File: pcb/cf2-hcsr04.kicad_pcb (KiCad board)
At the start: 2 copper layers, 25.2 x 27.3 mm, 9 parts, among them P1 CF_EXP_LEFT, P2 CF_EXP_RIGHT, U1 DS28E05, U2 REG71050, U3 HC-SR04

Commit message: First pcb draft
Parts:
- P1: footprint connectors:BF090-10-X-B2 -> connectors:BF090-10-X-B2-LEFT-NOPADS
- P2: footprint connectors:BF090-10-X-B2 -> connectors:BF090-10-X-B2-RIGHT-NOPADS
- moved U1 20.3 mm to (128.5, 103.9), turned to 90 degrees
- moved C2 9.99 mm to (140.5, 103.1), turned to 0 degrees
- moved U3 9.92 mm to (146.6, 97.0), turned to 270 degrees
- moved C1 2.29 mm to (141.7, 97.8)
- moved C3 0.37 mm to (135.9, 96.5)
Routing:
- net GND: track 22.8 -> 71.7 mm, vias 2 -> 0
- net /IO_4: track 49.7 -> 10.5 mm
- net /IO_1: track 5.67 -> 20.9 mm
- net /IO_2: track 5.37 -> 20.2 mm
- net /OW: track 18.8 -> 11.1 mm
- net /VCOM: track 13.8 -> 20.9 mm
- net N-0000021: track 9.82 -> 3.64 mm, vias 2 -> 0
- net N-0000022: track 24.3 -> 29.7 mm, vias 0 -> 4
- removed copper zone on B.Cu, net GND
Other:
- net class Default: clearance 0.1524 -> 0.0254; trace_width 0.2032 -> 0.508
- rule trace_clearance: 0.1524 -> 0.0254
- rule trace_min: 0.1524 -> 0.254

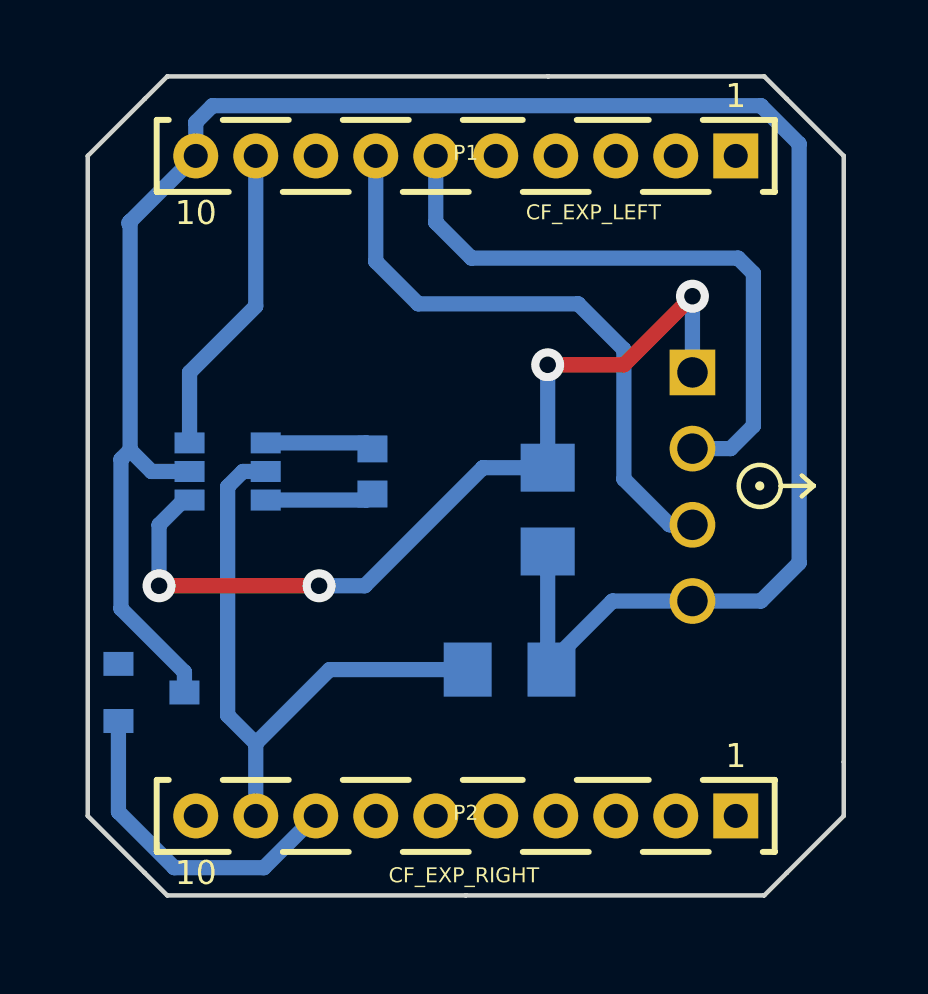
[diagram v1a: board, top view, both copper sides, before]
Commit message: Improved thickness of vias and other connections
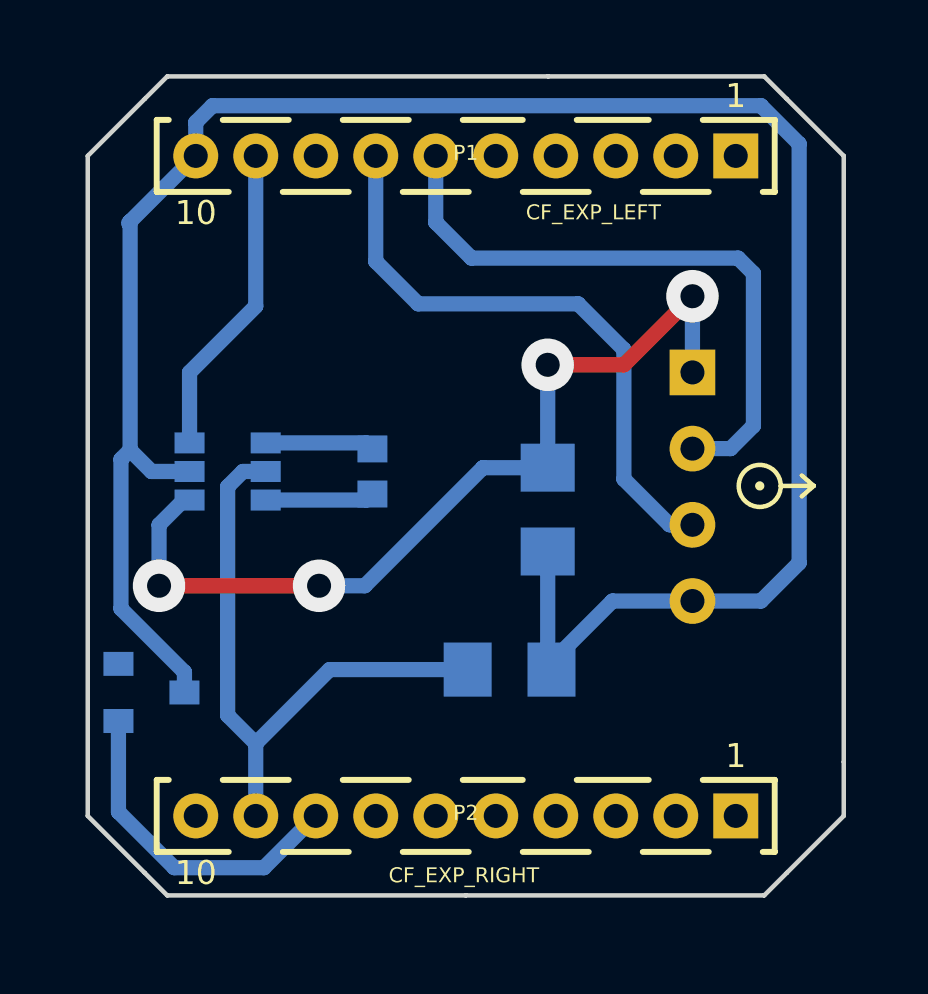
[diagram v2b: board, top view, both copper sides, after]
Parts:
- U3: footprint PIN_ARRAY_4x1 -> HC-SR04
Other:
- net class Default: via_dia 1.1 -> 1.75; via_drill 1 -> 0.8
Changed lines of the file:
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@@
     (segment_width 0.2)
     (edge_width 0.15)
-    (via_size 1.1)
-    (via_drill 1)
+    (via_size 1.75)
+    (via_drill 0.8)
     (via_min_size 0.635)
     (via_min_drill 0.381)
@@
     (mod_text_size 1 1)
     (mod_text_width 0.15)
-    (pad_size 1.5 1.5)
+    (pad_size 1.524 1.524)
     (pad_drill 0.8)
     (pad_to_mask_clearance 0)
@@
     (clearance 0.0254)
     (trace_width 0.508)
-    (via_dia 1.1)
-    (via_drill 1)
+    (via_dia 1.75)
+    (via_drill 0.8)
     (uvia_dia 0.6)
     (uvia_drill 0.5)
@@
       (scale (xyz 0.4 0.4 0.4))
       (rotate (xyz 0 0 180))
-    )
-  )
-  (module PIN_ARRAY_4x1 (layer B.Cu)
-    (at 146.558 97.028 270)
-    (descr "Double rangee de contacts 2 x 5 pins")
-    (tags CONN)
-    (fp_text reference U3 (at 0 2.54 270) (layer B.SilkS)
-      (effects (font (size 1.016 1.016) (thickness 0.2032)) (justify mirror))
-    )
-    (fp_text value HC-SR04 (at -0.254 2.54 270) (layer B.SilkS) hide
-      (effects (font (size 0.7 0.7) (thickness 0.15)) (justify mirror))
-    )
-    (fp_line (start 5.08 -1.27) (end -5.08 -1.27) (layer B.SilkS) (width 0.254))
-    (fp_line (start 5.08 1.27) (end -5.08 1.27) (layer B.SilkS) (width 0.254))
-    (fp_line (start -5.08 1.27) (end -5.08 -1.27) (layer B.SilkS) (width 0.254))
-    (fp_line (start 5.08 -1.27) (end 5.08 1.27) (layer B.SilkS) (width 0.254))
-    (pad 1 thru_hole rect (at -3.81 0 270) (size 1.524 1.524) (drill 1.016)
-      (layers *.Cu *.Mask B.SilkS)
-      (net 8 N-0000022)
-    )
-    (pad 2 thru_hole circle (at -1.27 0 270) (size 1.524 1.524) (drill 1.016)
-      (layers *.Cu *.Mask B.SilkS)
-      (net 1 /IO_1)
-    )
-    (pad 3 thru_hole circle (at 1.27 0 270) (size 1.524 1.524) (drill 1.016)
-      (layers *.Cu *.Mask B.SilkS)
-      (net 2 /IO_2)
-    )
-    (pad 4 thru_hole circle (at 3.81 0 270) (size 1.524 1.524) (drill 1.016)
-      (layers *.Cu *.Mask B.SilkS)
-      (net 6 GND)
-    )
-    (model pin_array\pins_array_4x1.wrl
-      (at (xyz 0 0 0))
-      (scale (xyz 1 1 1))
-      (rotate (xyz 0 0 0))
     )
   )
@@
     (pad 5 thru_hole circle (at -1 0 180) (size 1.5 1.5) (drill 0.8)
       (layers *.Cu *.Mask F.SilkS)
+    )
+  )
+  (module HC-SR04 (layer B.Cu)
+    (at 146.558 97.028 270)
+    (descr "Double rangee de contacts 2 x 5 pins")
+    (tags CONN)
+    (fp_text reference U3 (at 0 2.54 270) (layer B.SilkS)
+      (effects (font (size 1.016 1.016) (thickness 0.2032)) (justify mirror))
+    )
+    (fp_text value HC-SR04 (at 0 -2.54 270) (layer B.SilkS) hide
+      (effects (font (size 1.016 1.016) (thickness 0.2032)) (justify mirror))
+    )
+    (fp_line (start 5.08 -1.27) (end -5.08 -1.27) (layer B.SilkS) (width 0.254))
+    (fp_line (start 5.08 1.27) (end -5.08 1.27) (layer B.SilkS) (width 0.254))
+    (fp_line (start -5.08 1.27) (end -5.08 -1.27) (layer B.SilkS) (width 0.254))
+    (fp_line (start 5.08 -1.27) (end 5.08 1.27) (layer B.SilkS) (width 0.254))
+    (pad 1 thru_hole rect (at -3.81 0 270) (size 1.524 1.524) (drill 0.8)
+      (layers *.Cu *.Mask B.SilkS)
+      (net 8 N-0000022)
+    )
+    (pad 2 thru_hole circle (at -1.27 0 270) (size 1.524 1.524) (drill 0.8)
+      (layers *.Cu *.Mask B.SilkS)
+      (net 1 /IO_1)
+    )
+    (pad 3 thru_hole circle (at 1.27 0 270) (size 1.524 1.524) (drill 0.8)
+      (layers *.Cu *.Mask B.SilkS)
+      (net 2 /IO_2)
+    )
+    (pad 4 thru_hole circle (at 3.81 0 270) (size 1.524 1.524) (drill 0.8)
+      (layers *.Cu *.Mask B.SilkS)
+      (net 6 GND)
+    )
+    (model pin_array\pins_array_4x1.wrl
+      (at (xyz 0 0 0))
+      (scale (xyz 1 1 1))
+      (rotate (xyz 0 0 0))
     )
   )
@@
   (segment (start 146.558 93.218) (end 146.558 90.678) (width 0.508) (layer B.Cu) (net 8))
   (segment (start 141.732 92.964) (end 141.732 96.393) (width 0.508) (layer B.Cu) (net 8))
-  (via (at 141.732 92.964) (size 1.1) (layers F.Cu B.Cu) (net 8))
+  (via (at 141.732 92.964) (size 1.75) (layers F.Cu B.Cu) (net 8))
   (segment (start 144.272 92.964) (end 141.732 92.964) (width 0.508) (layer F.Cu) (net 8))
   (segment (start 146.558 90.678) (end 144.272 92.964) (width 0.508) (layer F.Cu) (net 8))
-  (via (at 146.558 90.678) (size 1.1) (layers F.Cu B.Cu) (net 8))
+  (via (at 146.558 90.678) (size 1.75) (layers F.Cu B.Cu) (net 8))
   (segment (start 134.112 100.33) (end 135.636 100.33) (width 0.508) (layer B.Cu) (net 8))
-  (via (at 128.778 100.33) (size 1.1) (layers F.Cu B.Cu) (net 8))
+  (via (at 128.778 100.33) (size 1.75) (layers F.Cu B.Cu) (net 8))
   (segment (start 128.778 100.33) (end 134.112 100.33) (width 0.508) (layer F.Cu) (net 8))
-  (via (at 134.112 100.33) (size 1.1) (layers F.Cu B.Cu) (net 8))
+  (via (at 134.112 100.33) (size 1.75) (layers F.Cu B.Cu) (net 8))
   (segment (start 128.778 98.298) (end 128.778 100.33) (width 0.508) (layer B.Cu) (net 8))
   (segment (start 129.6035 97.4725) (end 128.778 98.298) (width 0.508) (layer B.Cu) (net 8))

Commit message: Added side information and text to footprint (fixes #1)
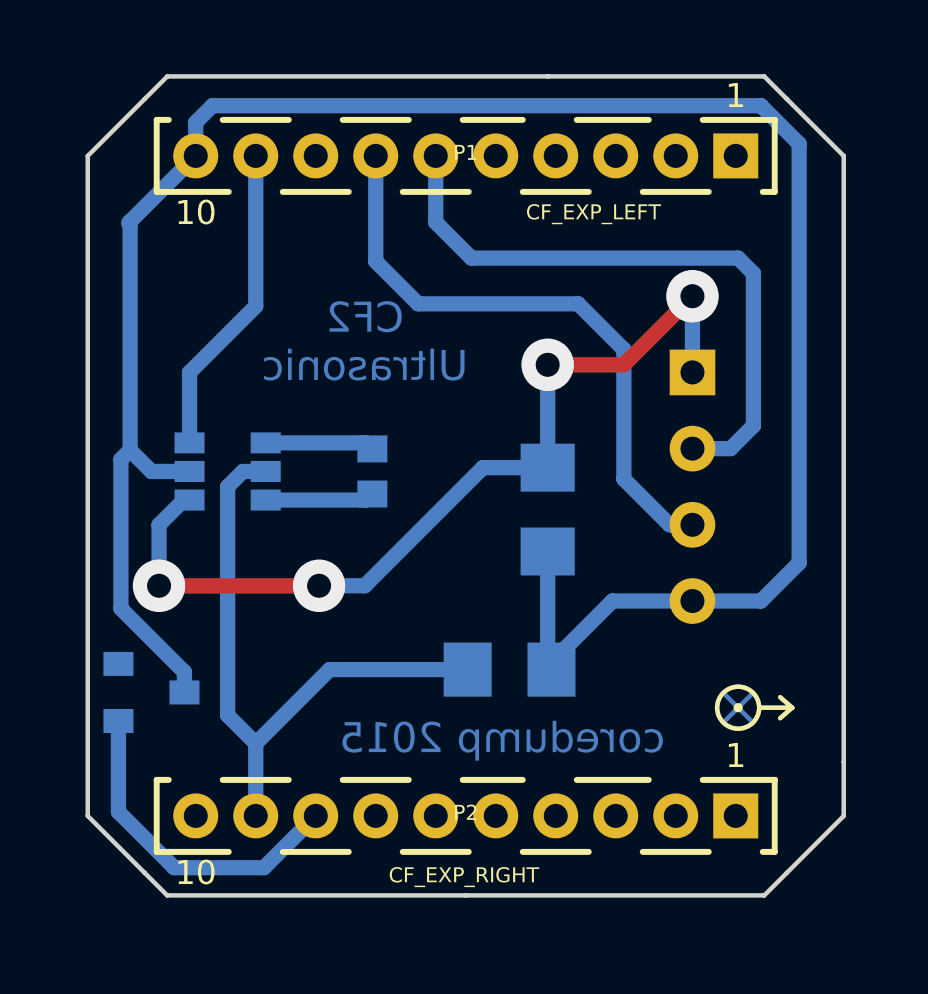
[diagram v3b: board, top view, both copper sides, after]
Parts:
- moved EXP_ORIENTATION 7.43 mm to (148.1, 104.4)
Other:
- board text added: "CF2 Ultrasonic"
- board text added: "coredump 2015"
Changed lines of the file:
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@@
     (area 82.650999 40.650919 195.351001 153.350921)
     (thickness 1.6)
-    (drawings 1896)
+    (drawings 1898)
     (tracks 66)
     (zones 0)
@@
   )
   (setup
-    (last_trace_width 0.508)
+    (last_trace_width 1)
     (user_trace_width 0.254)
     (user_trace_width 0.508)
@@
     )
   )
-  (module bitcraze:EXP_ORIENTATION_B_MASK (layer F.Cu)
-    (at 148.801 97.00092)
-    (fp_text reference EXP_ORIENTATION (at 0 1.925) (layer F.SilkS) hide
-      (effects (font (size 1 1) (thickness 0.15)))
-    )
-    (fp_text value VAL** (at 0.043 1.80508) (layer F.SilkS) hide
-      (effects (font (size 1 1) (thickness 0.15)))
-    )
-    (fp_line (start 0 0) (end -0.475 0.475) (layer B.Mask) (width 0.15))
-    (fp_line (start 0 0) (end 0.475 0.475) (layer B.Mask) (width 0.15))
-    (fp_line (start 0 0) (end 0.475 -0.475) (layer B.Mask) (width 0.15))
-    (fp_line (start 0 0) (end -0.475 -0.475) (layer B.Mask) (width 0.15))
-    (fp_circle (center 0 0) (end 0.7 0.025) (layer B.Mask) (width 0.15))
-    (fp_line (start 0.7 0) (end 1.8 0) (layer B.Mask) (width 0.15))
-    (fp_line (start 1.8 0) (end 1.4 -0.35) (layer B.Mask) (width 0.15))
-    (fp_line (start 1.8 0) (end 1.4 0.35) (layer B.Mask) (width 0.15))
-    (fp_line (start 1.8 0) (end 1.4 0.35) (layer F.SilkS) (width 0.15))
-    (fp_line (start 1.8 0) (end 1.4 -0.35) (layer F.SilkS) (width 0.15))
-    (fp_line (start 0.7 0) (end 1.8 0) (layer F.SilkS) (width 0.15))
-    (fp_circle (center 0 0) (end 0.7 0.025) (layer F.SilkS) (width 0.15))
-    (fp_circle (center 0 0) (end 0.075 0.025) (layer F.SilkS) (width 0.15))
-  )
   (module connectors:BF090-10-X-B2-LEFT-NOPADS (layer F.Cu)
     (at 139.001 86.00092 180)
@@
     )
   )
+  (module bitcraze:EXP_ORIENTATION_B_MASK (layer F.Cu)
+    (at 148.082 104.394)
+    (fp_text reference EXP_ORIENTATION (at 0 1.925) (layer F.SilkS) hide
+      (effects (font (size 1 1) (thickness 0.15)))
+    )
+    (fp_text value VAL** (at -1.27 -1.27) (layer F.SilkS) hide
+      (effects (font (size 1 1) (thickness 0.15)))
+    )
+    (fp_line (start 0 0) (end -0.475 0.475) (layer B.Cu) (width 0.15))
+    (fp_line (start 0 0) (end 0.475 0.475) (layer B.Cu) (width 0.15))
+    (fp_line (start 0 0) (end 0.475 -0.475) (layer B.Cu) (width 0.15))
+    (fp_line (start 0 0) (end -0.475 -0.475) (layer B.Cu) (width 0.15))
+    (fp_circle (center 0 0) (end 0.7 0.025) (layer B.Cu) (width 0.15))
+    (fp_line (start 0.7 0) (end 1.8 0) (layer B.Cu) (width 0.15))
+    (fp_line (start 1.8 0) (end 1.4 -0.35) (layer B.Cu) (width 0.15))
+    (fp_line (start 1.8 0) (end 1.4 0.35) (layer B.Cu) (width 0.15))
+    (fp_line (start 1.8 0) (end 1.4 0.35) (layer F.SilkS) (width 0.15))
+    (fp_line (start 1.8 0) (end 1.4 -0.35) (layer F.SilkS) (width 0.15))
+    (fp_line (start 0.7 0) (end 1.8 0) (layer F.SilkS) (width 0.15))
+    (fp_circle (center 0 0) (end 0.7 0.025) (layer F.SilkS) (width 0.15))
+    (fp_circle (center 0 0) (end 0.075 0.025) (layer F.SilkS) (width 0.15))
+  )
+  (gr_text "coredump 2015" (at 140.208 105.41) (layer B.Cu)
+    (effects (font (size 1 1) (thickness 0.25)) (justify mirror))
+  )
+  (gr_text "CF2\nUltrasonic" (at 135.636 92.202) (layer B.Cu)
+    (effects (font (size 1 1) (thickness 0.25)) (justify mirror))
+  )
   (gr_circle (center 171.751 129.75092) (end 148.251 129.75092) (layer Eco1.User) (width 0.2))

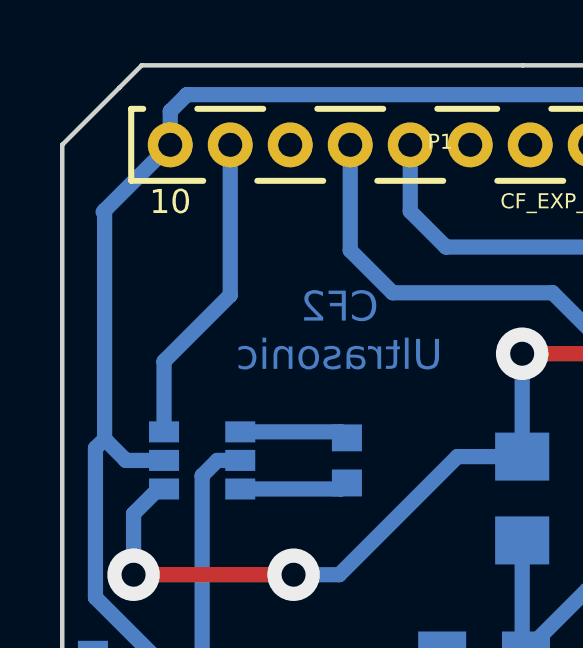
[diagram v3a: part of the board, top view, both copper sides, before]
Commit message: Removed acute angle
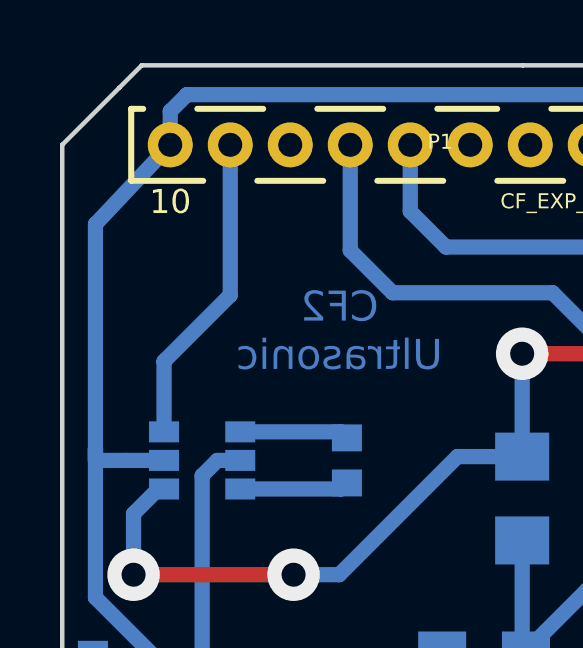
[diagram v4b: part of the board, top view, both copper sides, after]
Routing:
- net GND: track 71.7 -> 72.4 mm
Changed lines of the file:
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@@
     (thickness 1.6)
     (drawings 1898)
-    (tracks 66)
+    (tracks 65)
     (zones 0)
     (modules 9)
@@
   )
   (setup
-    (last_trace_width 1)
+    (last_trace_width 0.508)
     (user_trace_width 0.254)
     (user_trace_width 0.508)
@@
   (segment (start 131.572 96.52) (end 131.064 97.028) (width 0.508) (layer B.Cu) (net 5))
   (segment (start 129.62382 103.886) (end 129.62382 103.20782) (width 0.508) (layer B.Cu) (net 6))
-  (segment (start 127.508 96.11392) (end 127.81296 95.80896) (width 0.508) (layer B.Cu) (net 6))
+  (segment (start 127.508 96.11392) (end 127.508 96.52) (width 0.508) (layer B.Cu) (net 6))
   (segment (start 127.508 101.092) (end 127.508 96.11392) (width 0.508) (layer B.Cu) (net 6))
   (segment (start 129.62382 103.20782) (end 127.508 101.092) (width 0.508) (layer B.Cu) (net 6))
@@
   (segment (start 130.556 84.328) (end 148.844 84.328) (width 0.508) (layer B.Cu) (net 6))
   (segment (start 130.001 84.883) (end 130.556 84.328) (width 0.508) (layer B.Cu) (net 6))
-  (segment (start 127.81296 88.18896) (end 127.81296 95.80896) (width 0.508) (layer B.Cu) (net 6))
+  (segment (start 127.508 88.646) (end 127.508 96.52) (width 0.508) (layer B.Cu) (net 6))
   (segment (start 128.524 96.52) (end 129.794 96.52) (width 0.508) (layer B.Cu) (net 6))
-  (segment (start 127.81296 95.80896) (end 128.524 96.52) (width 0.508) (layer B.Cu) (net 6))
+  (segment (start 127.508 96.52) (end 128.524 96.52) (width 0.508) (layer B.Cu) (net 6))
   (segment (start 141.732 99.187) (end 141.732 102.997) (width 0.508) (layer B.Cu) (net 6) (status 10))
   (segment (start 141.732 102.997) (end 143.891 100.838) (width 0.508) (layer B.Cu) (net 6))
   (segment (start 143.891 100.838) (end 146.558 100.838) (width 0.508) (layer B.Cu) (net 6))
-  (segment (start 127.762 88.23992) (end 127.81296 88.18896) (width 0.508) (layer B.Cu) (net 6))
-  (segment (start 127.81296 88.18896) (end 130.001 86.00092) (width 0.508) (layer B.Cu) (net 6))
+  (segment (start 127.508 88.646) (end 130.001 86.00092) (width 0.508) (layer B.Cu) (net 6) (status 800000))
   (segment (start 132.334 97.4725) (end 135.68934 97.4725) (width 0.508) (layer B.Cu) (net 7))
   (segment (start 135.68934 97.4725) (end 135.89 97.27184) (width 0.508) (layer B.Cu) (net 7))
